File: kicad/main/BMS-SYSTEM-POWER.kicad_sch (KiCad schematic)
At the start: 81 parts, among them Q11 2N3904, Q12 2N3906_C49023424, U1 NCP1117ST33T3G, U21 AP64501SP-13, U22 AP64501SP-13, U23 BV1HAL45EFJ-E2, U24 AP64501SP-13, U8 BV1HAL45EFJ-E2

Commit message: Cliff/bumpers connector
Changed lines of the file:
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@@
 	(generator_version "10.0")
 	(paper "A2")
+	(rectangle
+		(start 38.1 170.18)
+		(end 54.61 222.25)
+		(stroke
+			(width 0)
+			(type solid)
+		)
+		(fill
+			(type color)
+			(color 132 0 0 1)
+		)
+	)
 	(text "POWER MANAGMENT"
 		(exclude_from_sim no)

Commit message: Second review round
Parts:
- added C148, C149, C150, C151: 10uF/25V, Capacitor_SMD:C_0603_1608Metric, symbol JLCImport:CL21A106KBYQNNE
- added D4: SS34_C8678, JLCImport:SS34_C8678, symbol JLCImport:SS34_C8678
- added R159: 10k, Resistor_SMD:R_0603_1608Metric, symbol Device:R_US
- added R160: 324k, Resistor_SMD:R_0603_1608Metric, symbol Device:R_US
- added U12: XRNR4030-10UH_M, JLCImport:XRNR4030-10UH_M, symbol JLCImport:XRNR4030-10UH_M
- added U5: MT3608, JLCImport:MT3608, symbol JLCImport:MT3608
- C104, C124, C127, C128, C129, C130, C131, C132, C144, C145, L4, R10, R154, R155, R156, R157, R23, U24: now not fitted
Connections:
- net GND: now also C148.2, C149.2, C150.2, C151.2, R159.1, U5.2 (GND)
- net VCC-5V-REG: now also C148.1, C149.1, U12.1, U5.4 (EN), U5.5 (IN)
- new net: D4.2 (A), U12.2, U5.1 (SW)
- new net: R159.2, R160.1, U5.3 (FB)
- new net VUS: C150.1, C151.1, D4.1 (K), R160.2
- no-connect marks 4 -> 5
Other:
- note added: "VOUT = 20V"
- moved on the sheet: C140, C141, R158, U1

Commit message: STM32 power rail switch
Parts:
- removed R150: 10k, Resistor_SMD:R_0603_1608Metric, symbol Device:R_US
- removed R151: 47k, Resistor_SMD:R_0603_1608Metric, symbol Device:R_US
- removed R158: 100, Resistor_SMD:R_0805_2012Metric, symbol Device:R_US
- removed U1: NCP1117ST33T3G, NCP1117ST33T3G:SOT230P700X180-4N, symbol NCP1117ST33T3G:NCP1117ST33T3G
- removed U8: BV1HAL45EFJ-E2, JLCImport:BV1HAL45EFJ-E2, symbol JLCImport:BV1HAL45EFJ-E2
- added 3.3V_SENSORS1: 3V3_SENSORS, oomwoo_altium:LED0603-B, symbol DesignLibrary:POWER_0_LED-SMD_DesignLibrary.SchLib
- added 5V1: (no value), oomwoo_altium:LED0603-B, symbol DesignLibrary:POWER_0_LED-SMD_DesignLibrary.SchLib
- added C126: 100nF/25V, Capacitor_SMD:C_0603_1608Metric, symbol Library:C_0603
- added C64: 10uF/6.3V, Capacitor_SMD:C_0603_1608Metric, symbol JLCImport:CL21A106KBYQNNE
- added D2: ZMM9V1_C2891750, JLCImport:ZMM9V1_C2891750, symbol JLCImport:ZMM9V1_C2891750
- added D39: SS34, Diode_SMD:D_SMA, symbol DesignLibrary:MAIN-BRUSH MOTOR_1_DIODE-2_DesignLibrary.SchLib
- added Q1, Q4: AOD407_C6396162, JLCImport:AOD407_C6396162, symbol JLCImport:AOD407_C6396162
- added Q16, Q17: AO3401, oomwoo_altium:SOT23-3D, symbol DesignLibrary:WATER-PUMP_1_mirrored_P-MOS-SOT23_DesignLibrary.SchLib
- added Q19: 2302V, JLCImport:2302V, symbol JLCImport:2302V
- added R102: 10k, Resistor_SMD:R_0603_1608Metric, symbol DesignLibrary:POWER_1_Resistor-1_DesignLibrary.SchLib
- added R165, R166, R168: 100k, Resistor_SMD:R_0603_1608Metric, symbol Device:R_US
- added R36, R42, R96, R97: 10, Resistor_SMD:R_0603_1608Metric, symbol Device:R_US
- added R89, R98: 1k, Resistor_SMD:R_0603_1608Metric, symbol DesignLibrary:POWER_2_Resistor-1_DesignLibrary.SchLib
- added R90, R91: 10k, Resistor_SMD:R_0603_1608Metric, symbol DesignLibrary:WATER-PUMP_2_Resistor-1_DesignLibrary.SchLib
- added U16: HT7533-1_C14289, JLCImport:HT7533-1_C14289, symbol JLCImport:HT7533-1_C14289
- C102, C107, C111, C117, C118, C119, C127, C128, C129: value 100nF/50V -> 100nF/25V; LCSC C1591 -> C1590; Manufacturer_Part_Number CL10B104KB8NNNC -> (none)
- C112, C120, C130: LCSC C1590 -> C107073; Manufacturer_Part_Number CL10B104KB8NNNC -> (none)
- C113, C114, C131, C132, C144, C145, C146: value 10uF/25V -> 10uF/6.3V; LCSC C96446 -> C1691
- C121, C122, C147, C148, C149, C63: value 10uF/25V -> 10uF/10V; LCSC C96446 -> C19702
- R10, R153, R16, R58, R59: LCSC (none) -> C2907088
- R14, R28: LCSC (none) -> C2907113; VOLTAGERATE * -> (none)
- R141, R146, R154: LCSC (none) -> C2907091
- R143, R148, R155: LCSC (none) -> C2930069
- R144, R156: LCSC (none) -> C2930012
- R145, R157: LCSC (none) -> C2960862
- R147: LCSC (none) -> C2907011
- R149: LCSC (none) -> C2907005
- R152, R159, R23: LCSC (none) -> C98220
- R160: LCSC (none) -> C5713284
- R29, R40: LCSC (none) -> C2907088; VOLTAGERATE * -> (none)
- R31, R32, R34, R45: LCSC (none) -> C98220; VOLTAGERATE * -> (none)
- renumbered D23 to 3.3V_STM1
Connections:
- net 3.3VBAT: now also U16.3 (Vout)
- net BAT-VCC: now also D2.1 (K), Q1.3 (S), Q4.3 (S), R165.1, R166.1
- net GND: now also Q19.2 (S), R168.1, R89.1, R98.1, U16.1 (GND)
- net POWER-BTN: now also C126.2, R102.1; no longer R45.1
- net POWER-EN: now also R16.1, U21.3 (EN); no longer U22.3 (EN)
- net V-MOTORS-EN: now also Q19.1 (G)
- net VCC-5V-REG: now also 5V1.1
- net VM-VBAT: now also Q1.2 (D), Q4.2 (D)
- net at D26.2 (K), D27.2 (K), Q12.2 (E)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: now also R102.2
- net at C140.1: now also D2.2 (A), U16.2 (Vin)
- removed net +3.3VP: R16.1, R23.1, U21.3 (EN)
- net VCC-3V3-P renamed VCC-3V3
- net VCC-3V3: now also Q16.2 (S), Q17.2 (S), R90.2, R91.2
- net VCC-CHARG renamed VCC-CHARGE
- new net: Q19.3 (D), R165.2, R166.2, R36.1, R42.1
- new net: Q1.1 (G), R36.2
- new net: C126.1, R45.1
- new net: Q17.1 (G), R97.2
- new net: Q4.1 (G), R42.2
- new net: 3.3V_SENSORS1.2, R98.2
- new net: 5V1.2, R89.2
- new net: Q16.1 (G), R96.2
- new net 3.3V-PI: R23.1
- new net 3.3V_EN: C64.2, D39.1 (A), R90.1, R91.1, R96.1, R97.1
- new net 5V_EN: R168.2, U22.3 (EN)
- new net VCC-3V3-REG: 3.3V_SENSORS1.1, C64.1, D39.2 (K), Q16.3 (D), Q17.3 (D)
- no-connect marks 5 -> 3
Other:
- moved on the sheet: 3.3V_STM1, C115, C116, C117, C118, C148, C149, C150, C151, C63, D24, D25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

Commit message: Update Power Control sch, Charger sch, Speaker + Mic, JTAG and Watch Dog
**Power Control:** Replaced the BJT with a MOSFET. The MCU hang condition is not covered yet.
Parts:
- removed C126: 100nF/25V, Capacitor_SMD:C_0603_1608Metric, symbol Library:C_0603
- removed C63: 10uF/10V, Capacitor_SMD:C_0603_1608Metric, symbol JLCImport:CL21A106KBYQNNE
- removed D24: 1N4148, oomwoo_altium:SOD123, symbol DesignLibrary:POWER_2_DIODE-1_DesignLibrary.SchLib
- removed D25, D26, D27, D28: 1N4148, oomwoo_altium:SOD123, symbol DesignLibrary:POWER_0_DIODE-1_DesignLibrary.SchLib
- removed D38: SS34, Diode_SMD:D_SMA, symbol DesignLibrary:MAIN-BRUSH MOTOR_1_DIODE-2_DesignLibrary.SchLib
- removed Q11: 2N3904, oomwoo_altium:SOT23-3D, symbol DesignLibrary:POWER_0_mirrored_NPN-SOT23_DesignLibrary.SchLib
- removed Q12: 2N3906_C49023424, JLCImport:2N3906_C49023424, symbol JLCImport:2N3906_C49023424
- removed R102, R45: 10k, Resistor_SMD:R_0603_1608Metric, symbol DesignLibrary:POWER_1_Resistor-1_DesignLibrary.SchLib
- removed R152: 10k, Resistor_SMD:R_0603_1608Metric, symbol Device:R_US
- removed R153, R59: 100k, Resistor_SMD:R_0603_1608Metric, symbol Device:R_US
- removed R28: 1k, Resistor_SMD:R_0603_1608Metric, symbol DesignLibrary:POWER_0_Resistor-1_DesignLibrary.SchLib
- removed R29, R40: 100k, Resistor_SMD:R_0603_1608Metric, symbol DesignLibrary:POWER_0_Resistor-1_DesignLibrary.SchLib
- removed R31: 10k, Resistor_SMD:R_0603_1608Metric, symbol DesignLibrary:POWER_0_Resistor-1_DesignLibrary.SchLib
- removed R32, R34: 10k, Resistor_SMD:R_0603_1608Metric, symbol DesignLibrary:POWER_2_Resistor-1_DesignLibrary.SchLib
- removed U23: BV1HAL45EFJ-E2, JLCImport:BV1HAL45EFJ-E2, symbol JLCImport:BV1HAL45EFJ-E2
- added C14, C22: 1uF/25V, symbol Device:C_Small
- added C65: 10uF/25V, Capacitor_SMD:C_0603_1608Metric, symbol JLCImport:CL21A106KBYQNNE
- added D26: 1N4148, oomwoo_altium:SOD123, symbol DesignLibrary:POWER_2_DIODE-1_DesignLibrary.SchLib
- added D40: SS34, Diode_SMD:D_SMA, symbol DesignLibrary:MAIN-BRUSH MOTOR_1_DIODE-2_DesignLibrary.SchLib
- added Q13: NP3407MR-G, JLCImport:NP3407MR-G, symbol JLCImport:NP3407MR-G
- added Q21, Q23: 2302V, JLCImport:2302V, symbol JLCImport:2302V
- added Q5, Q6: AOD407_C6396162, JLCImport:AOD407_C6396162, symbol JLCImport:AOD407_C6396162
- added R167, R169, R171, R76: 100k, Resistor_SMD:R_0603_1608Metric, symbol Device:R_US
- added R172, R173, R67: 10k, Resistor_SMD:R_0603_1608Metric, symbol Device:R_US
- added R79, R88: 10, Resistor_SMD:R_0603_1608Metric, symbol Device:R_US
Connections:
- net BAT-VCC: now also Q13.2 (S), R171.2, R67.1
- net GND: now also C22.2, C65.2, D40.1 (A), Q21.2 (S), Q23.2 (S), R76.2
- net POWER-BTN: now also C14.2, D26.2 (K), R67.2
- net POWER-EN: now also Q13.3 (D)
- net PWR-BTN-SENSE: now also D26.1 (A), R173.1
- net STM-PWR-CTRL: now also Q23.1 (G), R172.1
- net V-MOTORS-EN: now also Q21.1 (G), R76.1
- net VCC-3V3: now also R172.2, R173.2
- net VCC-5V-REG: now also Q5.3 (S), Q6.3 (S), R167.1, R169.1
- net VM-5V: now also C65.1, D40.2 (K), Q5.2 (D), Q6.2 (D)
- new net: C14.1, C22.1, Q13.1 (G), Q23.3 (D), R171.1
- new net: Q21.3 (D), R167.2, R169.2, R79.1, R88.1
- new net: Q6.1 (G), R88.2
- new net: Q5.1 (G), R79.2
- no-connect marks 3 -> 1
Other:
- moved on the sheet: 3.3V_SENSORS1, C148, C149, C150, C151, C62, C64, D37, D39, D4, Q1, Q16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

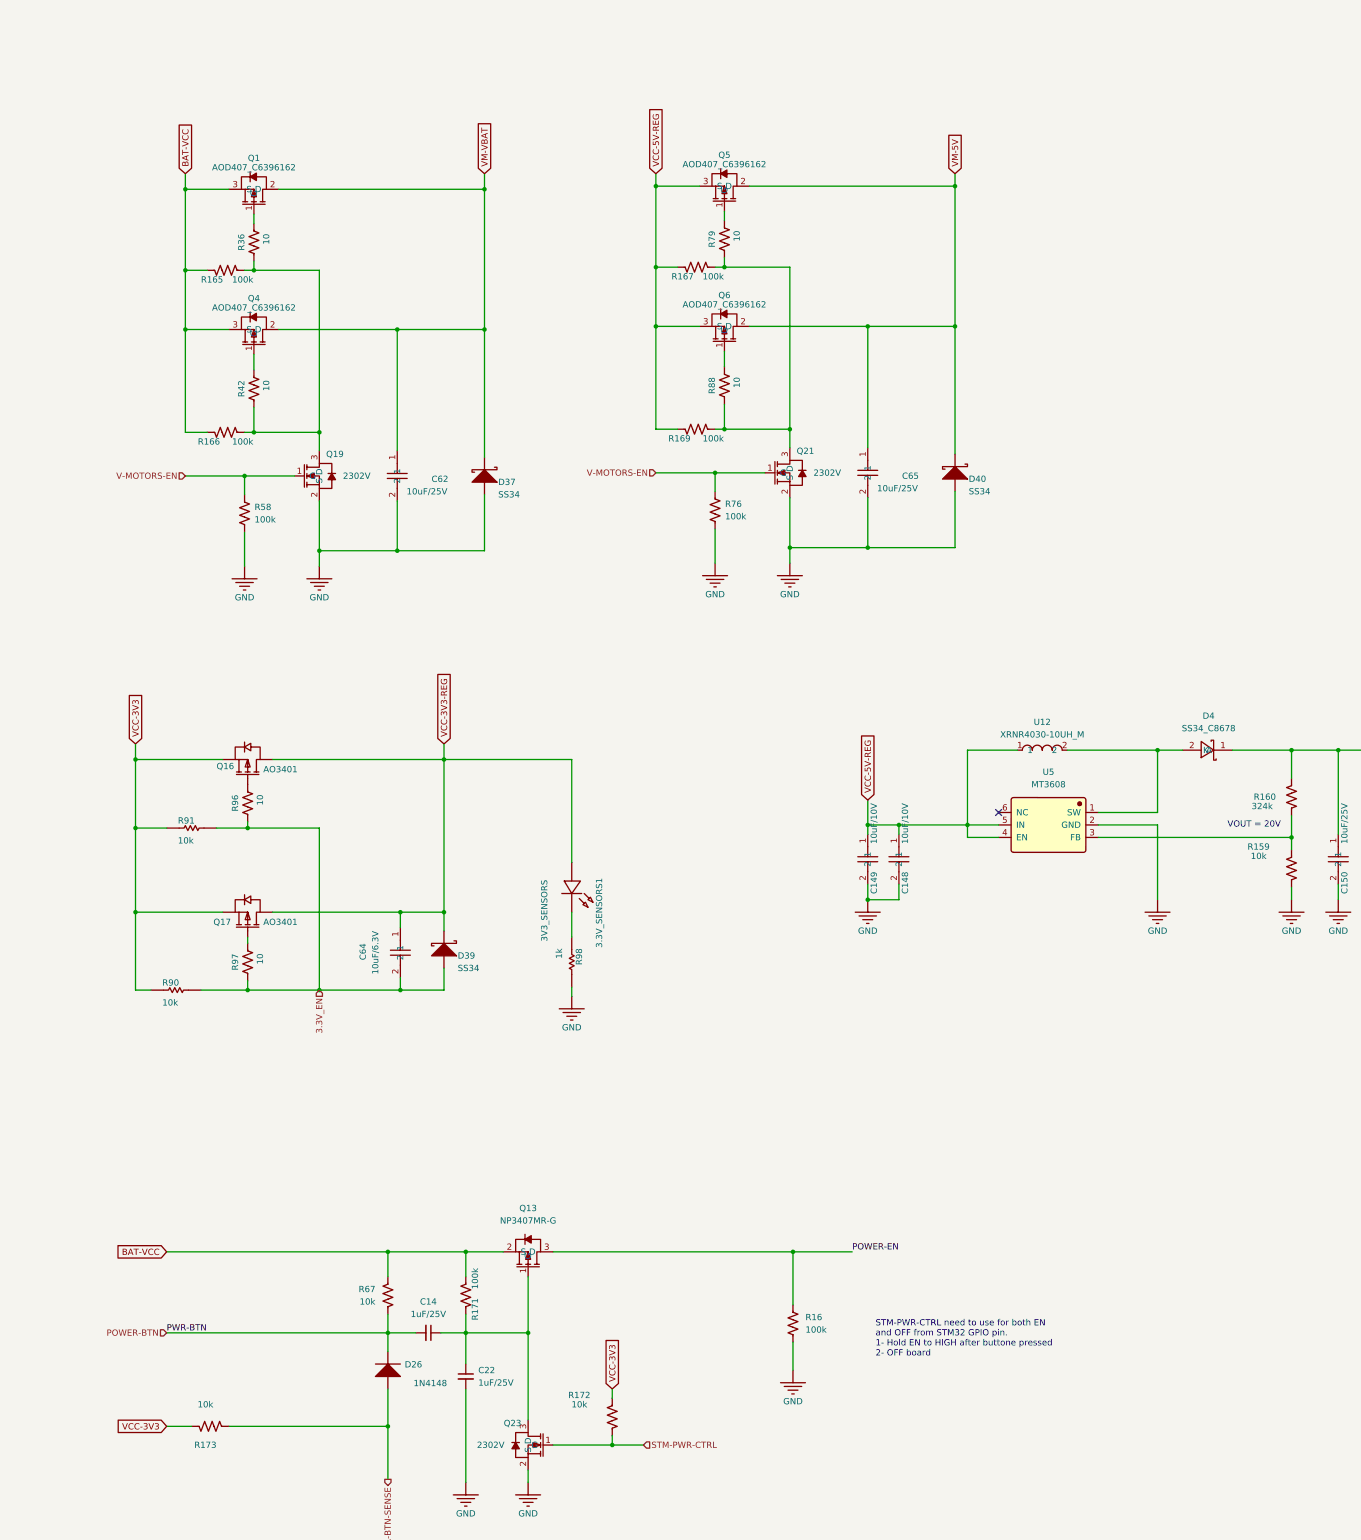
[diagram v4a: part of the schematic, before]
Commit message: Remove VM-5V; add VM-VBAT watchdog safety
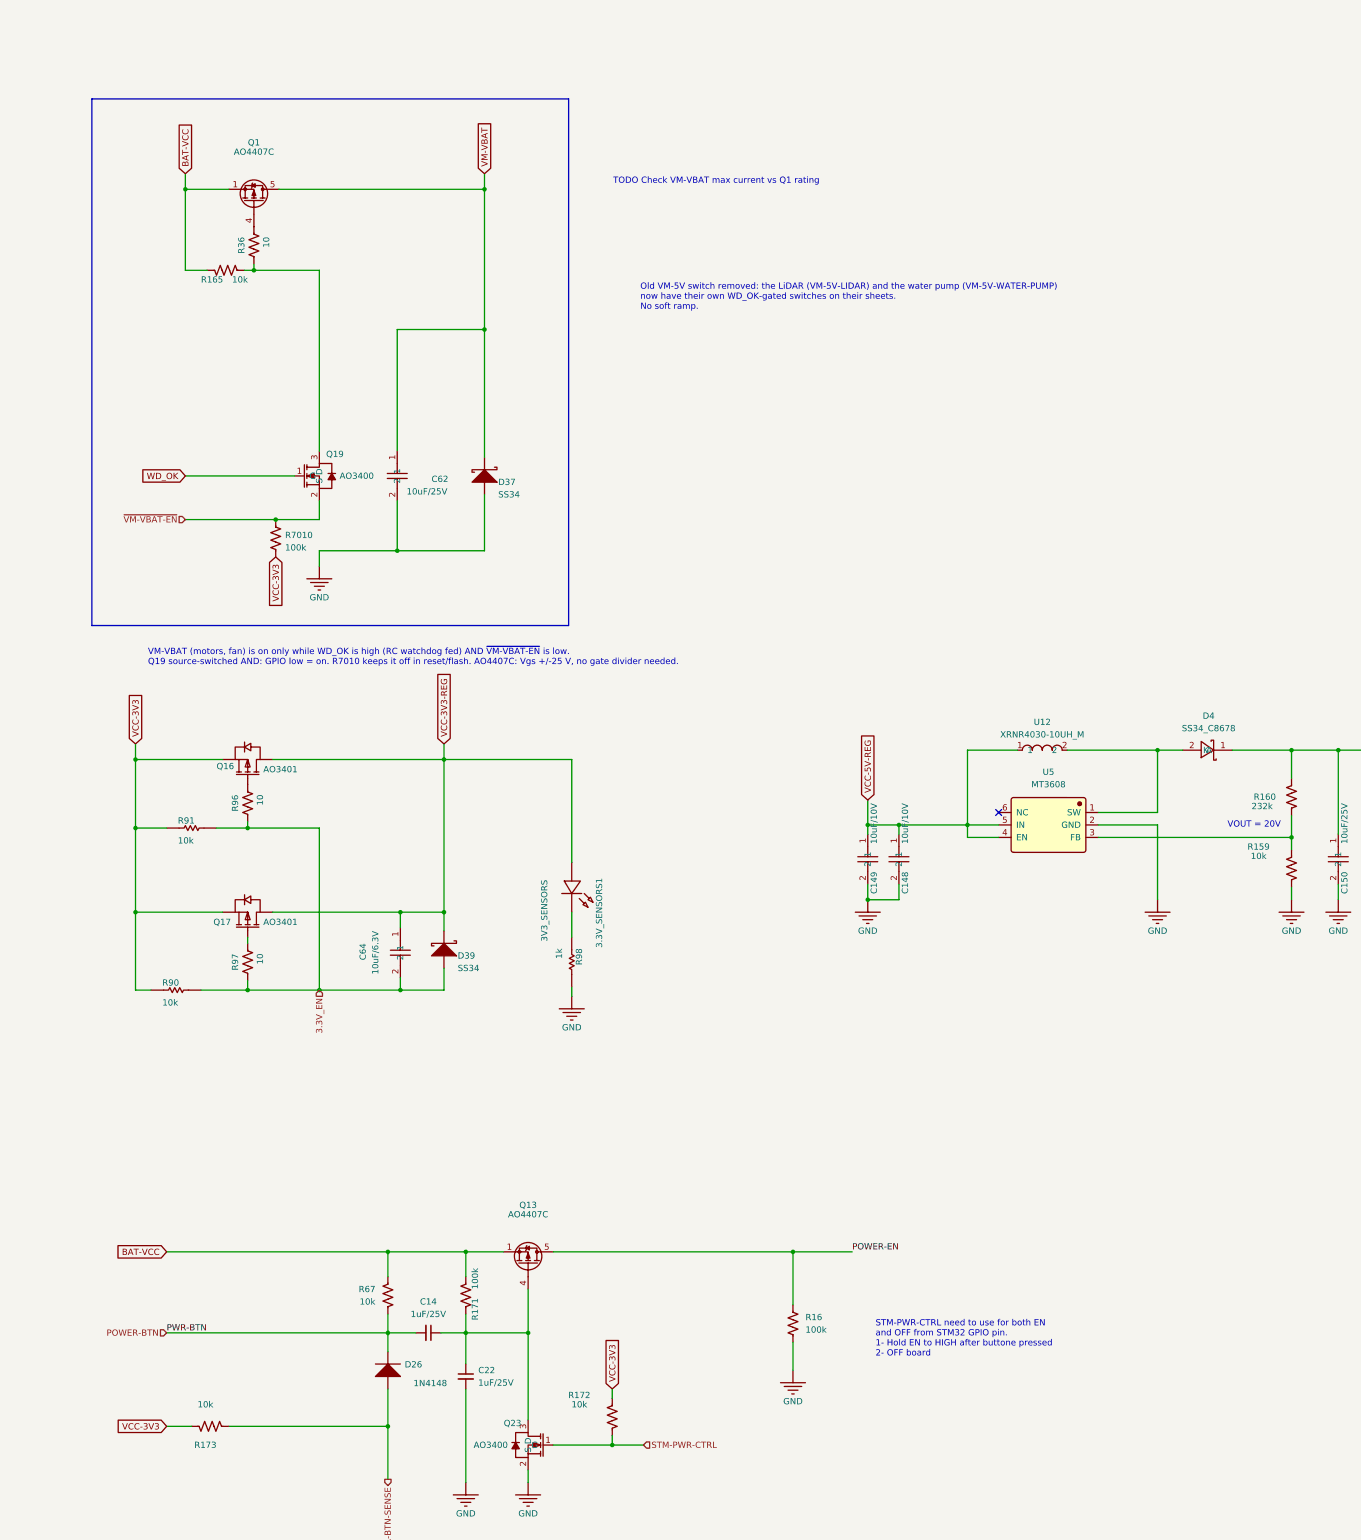
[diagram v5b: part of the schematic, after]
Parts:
- removed C65: 10uF/25V, Capacitor_SMD:C_0603_1608Metric, symbol JLCImport:CL21A106KBYQNNE
- removed D40: SS34, Diode_SMD:D_SMA, symbol DesignLibrary:MAIN-BRUSH MOTOR_1_DIODE-2_DesignLibrary.SchLib
- removed Q21: 2302V, JLCImport:2302V, symbol JLCImport:2302V
- removed Q4, Q5, Q6: AOD407_C6396162, JLCImport:AOD407_C6396162, symbol JLCImport:AOD407_C6396162
- removed R166, R167, R169, R58, R76: 100k, Resistor_SMD:R_0603_1608Metric, symbol Device:R_US
- removed R42, R79, R88: 10, Resistor_SMD:R_0603_1608Metric, symbol Device:R_US
- added R7010: 100k, Resistor_SMD:R_0603_1608Metric, symbol Device:R_US
- Q1: value AOD407_C6396162 -> AO4407C; footprint JLCImport:AOD407_C6396162 -> Package_SO:SOIC-8_3.9x4.9mm_P1.27mm; symbol JLCImport:AOD407_C6396162 -> JLCImport:AO4407C; LCSC C6396162 -> C469397; Manufacturer JSMSEMI -> Alpha & Omega Semicon; Manufacturer Part AOD407 -> AO4407C
- Q13: value NP3407MR-G -> AO4407C; footprint JLCImport:NP3407MR-G -> Package_SO:SOIC-8_3.9x4.9mm_P1.27mm; symbol JLCImport:NP3407MR-G -> JLCImport:AO4407C; LCSC C2991124 -> C469397; Manufacturer NATLINEAR -> Alpha & Omega Semicon; Manufacturer Part NP3407MR-G -> AO4407C
- Q16, Q17: LCSC C15127 -> C20628875; Manufacturer * -> FOSAN
- Q19, Q23: value 2302V -> AO3400; footprint JLCImport:2302V -> JLCImport:AO3400; symbol JLCImport:2302V -> JLCImport:AO3400; LCSC C7431443 -> C20628874; Manufacturer HL -> FOSAN; Manufacturer Part 2302V -> AO3400
- R160: value 324k -> 232k; LCSC C5713284 -> C22913
- R165: value 100k -> 10k; LCSC C2907088 -> C98220
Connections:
- net BAT-VCC: now also Q1.1 (S), Q1.2 (S), Q13.1 (S), Q13.3 (S)
- net GND: no longer Q19.2 (S)
- net POWER-EN: now also Q13.5 (D), Q13.6 (D), Q13.7 (D), Q13.8 (D); no longer Q13.3 (D)
- net VCC-3V3: now also R7010.2
- net VM-VBAT: now also Q1.5 (D), Q1.6 (D), Q1.7 (D), Q1.8 (D); no longer Q1.2 (D)
- net at C14.1, C22.1, Q23.3 (D)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: now also Q13.4 (G); no longer Q13.1 (G)
- net at R36.2: now also Q1.4 (G); no longer Q1.1 (G)
- net V-MOTORS-EN renamed WD_OK
- new net ~{VM-VBAT-EN}: Q19.2 (S), R7010.1
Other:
- note added: "Old VM-5V switch removed: the LiDAR (VM-5V-LIDAR) and the water pump (VM-5V-WATER-PUMP) now have their own WD_OK-gated switches on their sheets. No soft ramp."
- note added: "TODO Check VM-VBAT max current vs Q1 rating"
- note added: "VM-VBAT (motors, fan) is on only while WD_OK is high (RC watchdog fed) AND ~{VM-VBAT-EN} is low. Q19 source-switched AND: GPIO low = on. R7010 keeps it off in reset/flash. AO4407C: Vgs +/-25 V, no gate divider needed."
- moved on the sheet: R36
